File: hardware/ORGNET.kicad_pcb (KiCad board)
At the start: 2 copper layers, 21 x 50 mm, 41 parts, among them J1 Conn_02x08_Odd_Even, J3 Conn_01x03, U1 SN74LVC8T245, U2 SN74LVC8T245, U3 AP2112K-3.3, U4 RP2350A, U5 W25Q128JVP, U6 Raspberry Pi Radio Module 2, Y1 12M

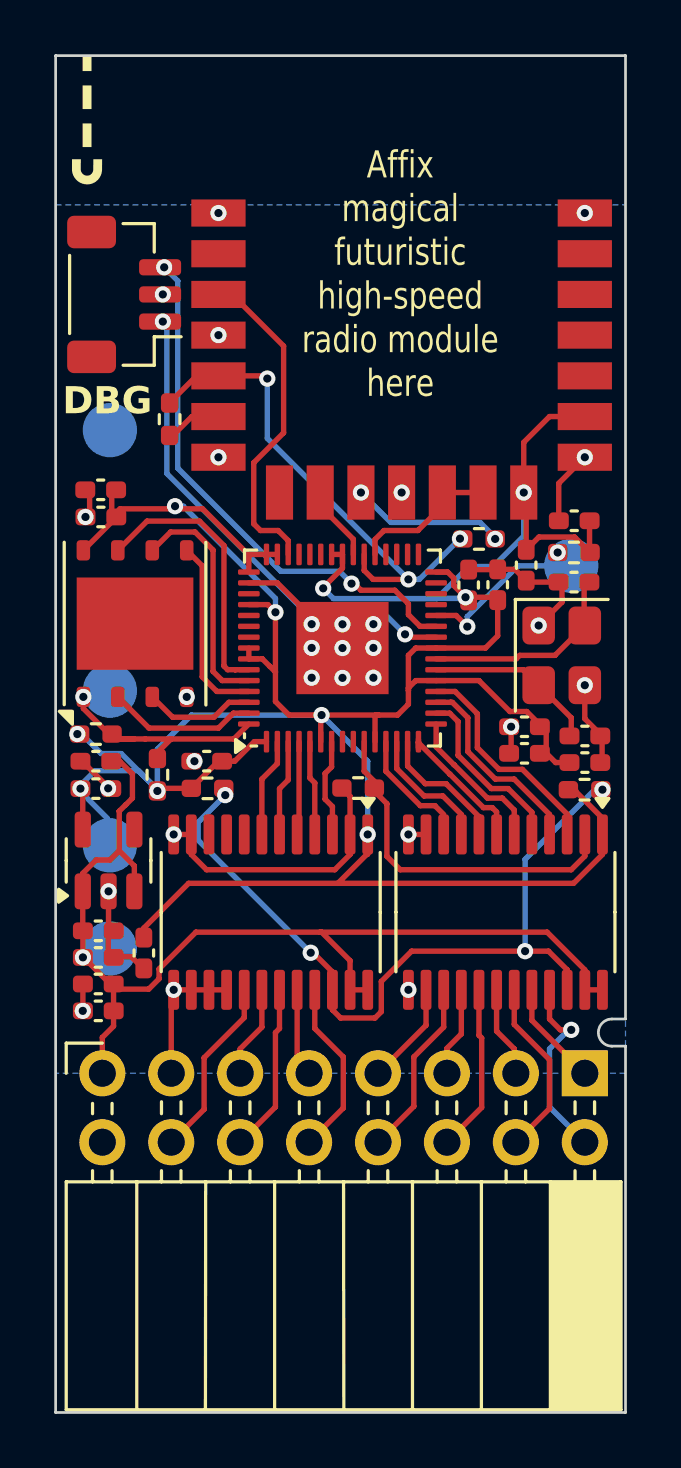
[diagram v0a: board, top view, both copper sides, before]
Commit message: Fix power routing to address short circuiting issue
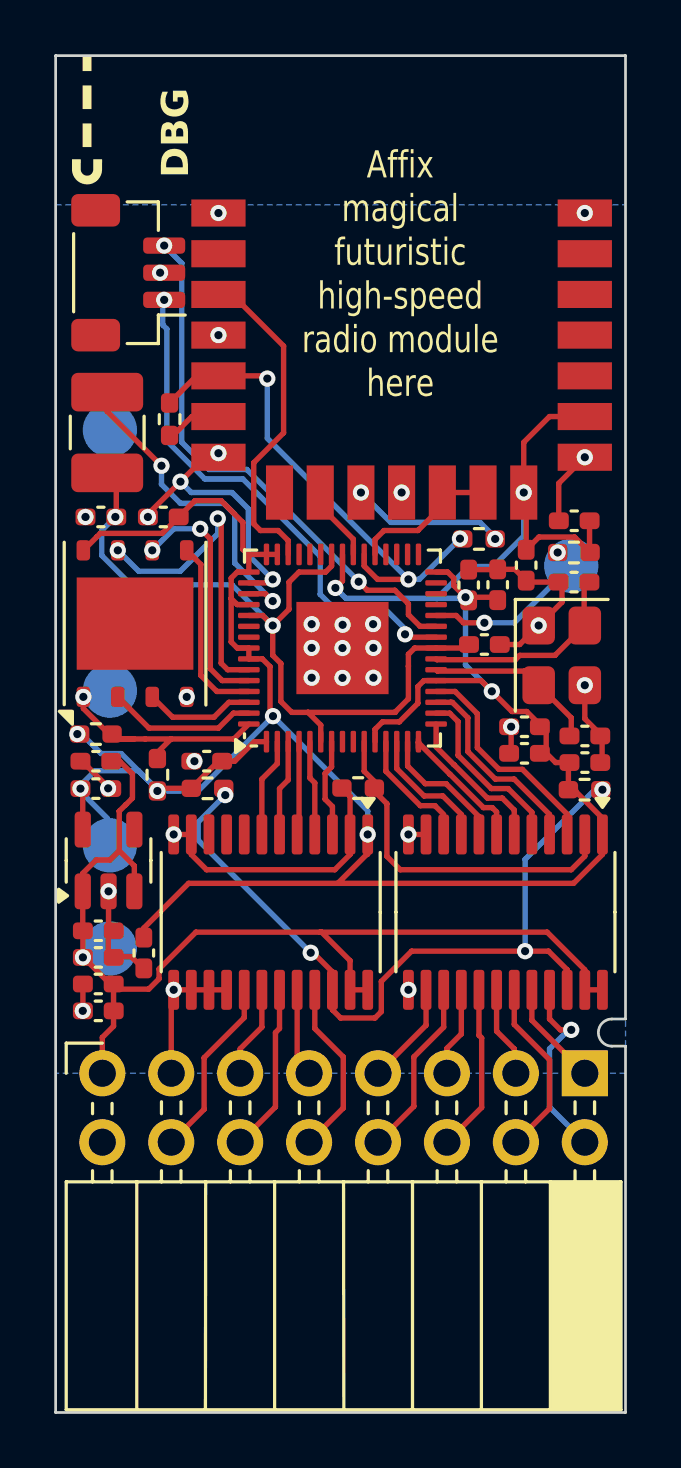
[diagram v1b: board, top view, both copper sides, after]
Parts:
- added C20: 22u, Capacitor_SMD:C_0402_1005Metric_Pad0.74x0.62mm_HandSolder, F.Cu at (157.8, 95.4)
- added L1: 3.3u, Inductor_SMD:L_1210_3225Metric_Pad1.42x2.65mm_HandSolder, F.Cu at (143.9, 87.6)
- moved C16 2.51 mm to (146.0, 90.7)
- moved J3 0.81 mm to (144.7, 81.7)
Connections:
- C17 pad 2: +3V3 -> Net-(U4-VREG_FB)
- U4 pad 23: +3V3 -> Net-(U4-VREG_FB)
- U4 pad 39: +3V3 -> Net-(U4-VREG_FB)
- U4 pad 48: unconnected-(U4-VREG_LX-Pad48) -> Net-(U4-VREG_LX)
- U4 pad 50: unconnected-(U4-VREG_FB-Pad50) -> Net-(U4-VREG_FB)
- U4 pad 6: +3V3 -> Net-(U4-VREG_FB)
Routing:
- net Net-(U4-VREG_FB): track 0.00 -> 29.5 mm, vias 0 -> 2
- net +3V3: track 123.9 -> 110.1 mm, vias 10 -> 9
- net Net-(U4-VREG_LX): track 0.00 -> 12.2 mm, vias 0 -> 2
- net GND: track 40.3 -> 47.2 mm, vias 29 -> 32
- net Net-(U4-QSPI_SD3): track 10.1 -> 11.6 mm, vias 0 -> 2
- net DBG_SWCLK: track 18.1 -> 19.2 mm
- net Net-(U4-QSPI_SCLK): track 8.73 -> 9.00 mm, vias 0 -> 2
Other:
- board text added: "V1.1"
- board text removed: "V1"
